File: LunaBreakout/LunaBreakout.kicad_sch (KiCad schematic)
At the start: 35 parts, among them J2 Conn_01x03, J6 USB_C_Receptacle_USB2.0_16P, SW1 SW_SPST, U1 RP2040, U2 AMS1117-3.3, U3 W25Q32JVSS, Y1 12Mhz

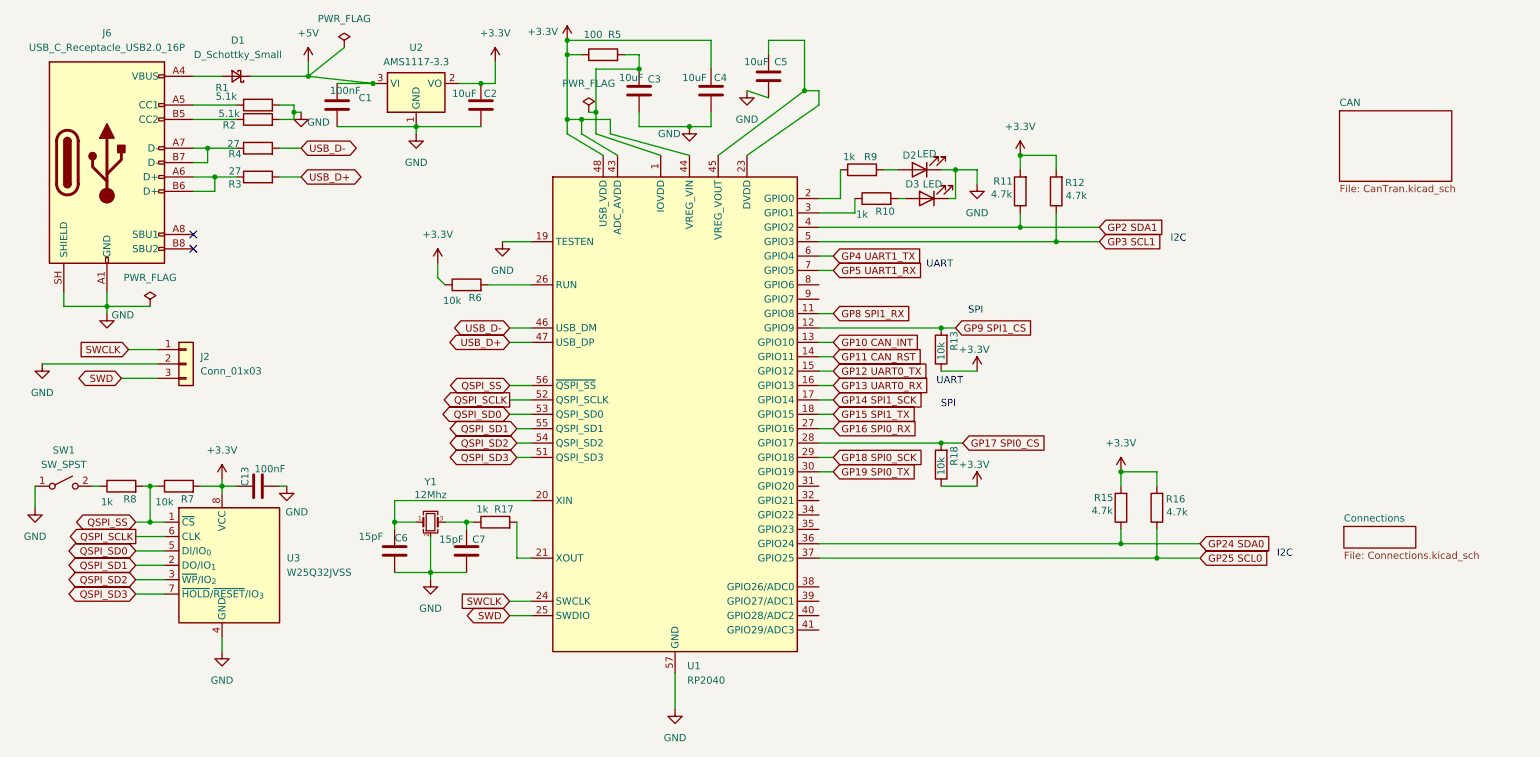
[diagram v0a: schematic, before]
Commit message: Took CAN out of schematic, changes connectorst, added misc connectors and external power symbol
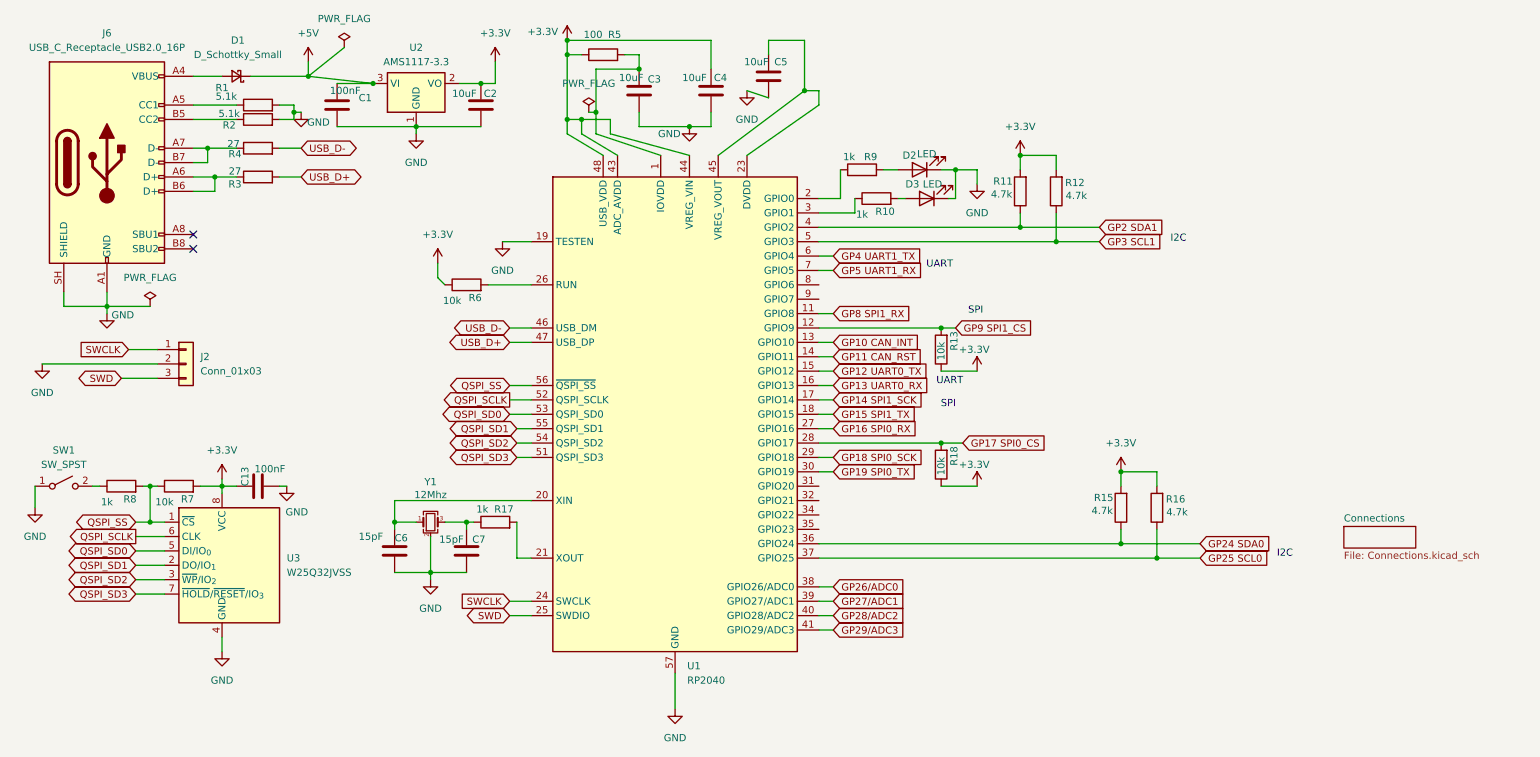
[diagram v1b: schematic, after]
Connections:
- net GP26/ADC0: now reaches U1.38 (GPIO26/ADC0)
- net GP27/ADC1: now reaches U1.39 (GPIO27/ADC1)
- net GP28/ADC2: now reaches U1.40 (GPIO28/ADC2)
- net GP29/ADC3: now reaches U1.41 (GPIO29/ADC3)
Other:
- removed sheet CAN
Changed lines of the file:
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@@
 	(wire
 		(pts
+			(xy 153.67 123.19) (xy 156.21 123.19)
+		)
+		(stroke
+			(width 0)
+			(type default)
+		)
+	)
+	(wire
+		(pts
 			(xy 63.5 27.94) (xy 63.5 25.4)
 		)
@@
 	(wire
 		(pts
+			(xy 153.67 125.73) (xy 156.21 125.73)
+		)
+		(stroke
+			(width 0)
+			(type default)
+		)
+	)
+	(wire
+		(pts
 			(xy 177.8 72.39) (xy 175.26 72.39)
 		)
@@
 	(wire
 		(pts
+			(xy 153.67 120.65) (xy 156.21 120.65)
+		)
+		(stroke
+			(width 0)
+			(type default)
+		)
+	)
+	(wire
+		(pts
 			(xy 153.67 54.61) (xy 189.23 54.61)
 		)
@@
 	(wire
 		(pts
+			(xy 153.67 118.11) (xy 156.21 118.11)
+		)
+		(stroke
+			(width 0)
+			(type default)
+		)
+	)
+	(wire
+		(pts
 			(xy 181.61 44.45) (xy 181.61 46.99)
 		)
@@
 		)
 	)
+	(global_label "GP27{slash}ADC1"
+		(shape input)
+		(at 156.21 120.65 0)
+		(fields_autoplaced yes)
+		(effects
+			(font
+				(size 1.27 1.27)
+			)
+			(justify left)
+		)
+		(property "Intersheetrefs" "${INTERSHEET_REFS}"
+			(at 170.3228 120.65 0)
+			(hide yes)
+			(show_name no)
+			(do_not_autoplace no)
+			(effects
+				(font
+					(size 1.27 1.27)
+				)
+				(justify left)
+			)
+		)
+	)
 	(global_label "GP15 SPI1_TX"
 		(shape input)
@@
 		)
 	)
+	(global_label "GP29{slash}ADC3"
+		(shape input)
+		(at 156.21 125.73 0)
+		(fields_autoplaced yes)
+		(effects
+			(font
+				(size 1.27 1.27)
+			)
+			(justify left)
+		)
+		(property "Intersheetrefs" "${INTERSHEET_REFS}"
+			(at 170.3228 125.73 0)
+			(hide yes)
+			(show_name no)
+			(do_not_autoplace no)
+			(effects
+				(font
+					(size 1.27 1.27)
+				)
+				(justify left)
+			)
+		)
+	)
+	(global_label "GP26{slash}ADC0"
+		(shape input)
+		(at 156.21 118.11 0)
+		(fields_autoplaced yes)
+		(effects
+			(font
+				(size 1.27 1.27)
+			)
+			(justify left)
+		)
+		(property "Intersheetrefs" "${INTERSHEET_REFS}"
+			(at 170.3228 118.11 0)
+			(hide yes)
+			(show_name no)
+			(do_not_autoplace no)
+			(effects
+				(font
+					(size 1.27 1.27)
+				)
+				(justify left)
+			)
+		)
+	)
 	(global_label "GP17 SPI0_CS"
 		(shape input)
@@
 		)
 	)
+	(global_label "GP28{slash}ADC2"
+		(shape input)
+		(at 156.21 123.19 0)
+		(fields_autoplaced yes)
+		(effects
+			(font
+				(size 1.27 1.27)
+			)
+			(justify left)
+		)
+		(property "Intersheetrefs" "${INTERSHEET_REFS}"
+			(at 170.3228 123.19 0)
+			(hide yes)
+			(show_name no)
+			(do_not_autoplace no)
+			(effects
+				(font
+					(size 1.27 1.27)
+				)
+				(justify left)
+			)
+		)
+	)
 	(global_label "USB_D+"
 		(shape bidirectional)
@@
 				)
 			)
-		)
-	)
-	(sheet
-		(at 245.618 34.036)
-		(size 19.812 12.446)
-		(exclude_from_sim no)
-		(in_bom yes)
-		(on_board yes)
-		(dnp no)
-		(fields_autoplaced yes)
-		(stroke
-			(width 0.1524)
-			(type solid)
-		)
-		(fill
-			(color 0 0 0 0)
-		)
-		(property "Sheetname" "CAN"
-			(at 245.618 33.3244 0)
-			(show_name no)
-			(do_not_autoplace no)
-			(effects
-				(font
-					(size 1.27 1.27)
-				)
-				(justify left bottom)
-			)
-		)
-		(property "Sheetfile" "CanTran.kicad_sch"
-			(at 245.618 47.0666 0)
-			(show_name no)
-			(do_not_autoplace no)
-			(effects
-				(font
-					(size 1.27 1.27)
-				)
-				(justify left top)
-			)
-		)
-		(instances
-			(project "LunaBreakout"
-				(path "/5f8915c9-c09e-4522-819d-9a09dec9e693"
-					(page "2")
-				)
-			)

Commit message: Started on layout and traces
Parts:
- added R19, R20, R21, R22: 10k, Resistor_SMD:R_0805_2012Metric, symbol Device:R
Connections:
- net +3.3V: now also R19.1, R20.1, R21.1, R22.1
- net GP20: now reaches U1.31 (GPIO20)
- net GP20: now also R19.2
- net GP21: now reaches U1.32 (GPIO21)
- net GP21: now also R20.2
- net GP22: now reaches U1.34 (GPIO22)
- net GP22: now also R21.2
- net GP23: now reaches U1.35 (GPIO23)
- net GP23: now also R22.2
- net GP10 CAN_INT: no longer names the net of U1.13 (GPIO10)
- net GP11 CAN_RST: no longer names the net of U1.14 (GPIO11)
- no-connect marks 2 -> 6
